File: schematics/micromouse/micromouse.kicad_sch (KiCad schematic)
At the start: 61 parts, among them J1 TOF_LEFT, J10 MotorB_Conn, J11 BMI_ConnB, J12 BMI_ConnA, J13 StepDown_{In+}, J14 StepDown_{In-}, J15 StepDown_{Out+}, J16 StepDown_{Out-}, J2 TOF_FRONTLEFT, J3 TOF_FRONTRIGHT, J4 TOF_RIGHT, J5 BatteryConnector, J6 PMW3360_Conn, J7 Bluetooth_Conn, J8 Programming_Conn, J9 MotorA_Conn, SW1 SW_SPDT, SW2 PB_RESET, SW3 PB_BOOT, SW4 SW_DIP_x04, U1 STM32F103CBTx, U2 DRV8833PWP, U3 AMS1117-3.3, U4 PCF8574TS, U5 PCF8574TS, U6 W25Q32JVSS, Y1 Crystal (8MHz), Y2 Crystal (8MHz)

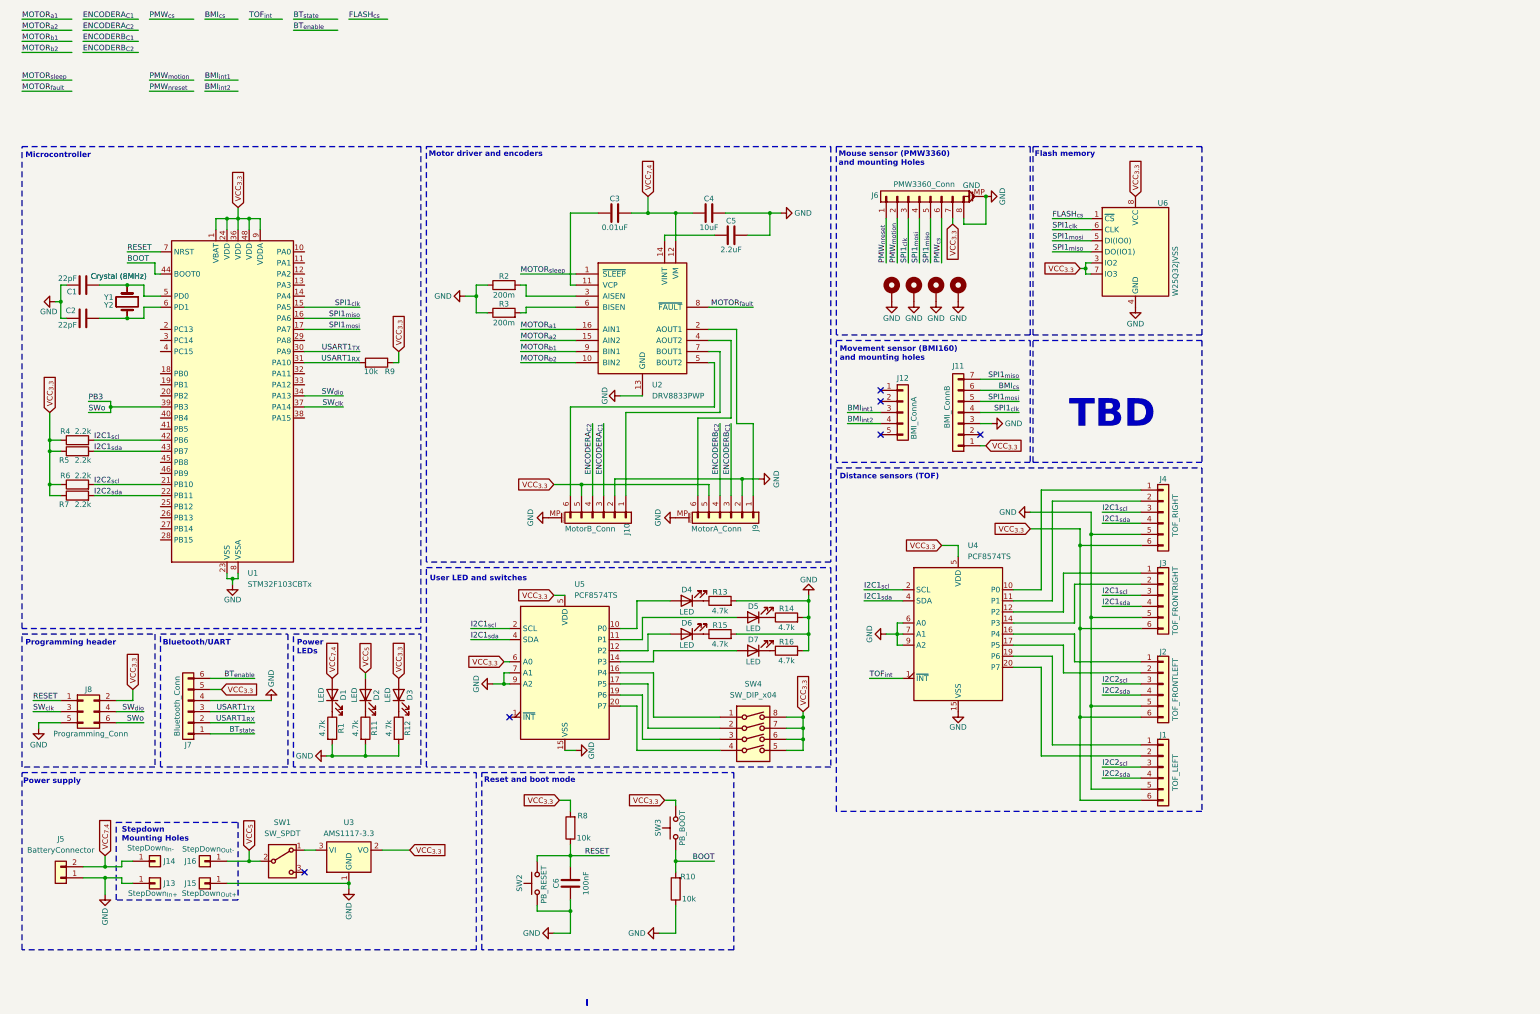
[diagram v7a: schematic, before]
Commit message: Schematic: * Reorganize STM32 pinout due to Software needs/mititations * Add PCB power protection diodes for Battery port and  Programming port.
PCB:
* Redistribute all lines
* Avoid Crystal zone with SPI/I2C lines
* Add text for element's pinouts

TODO: Add Test Points for signals?
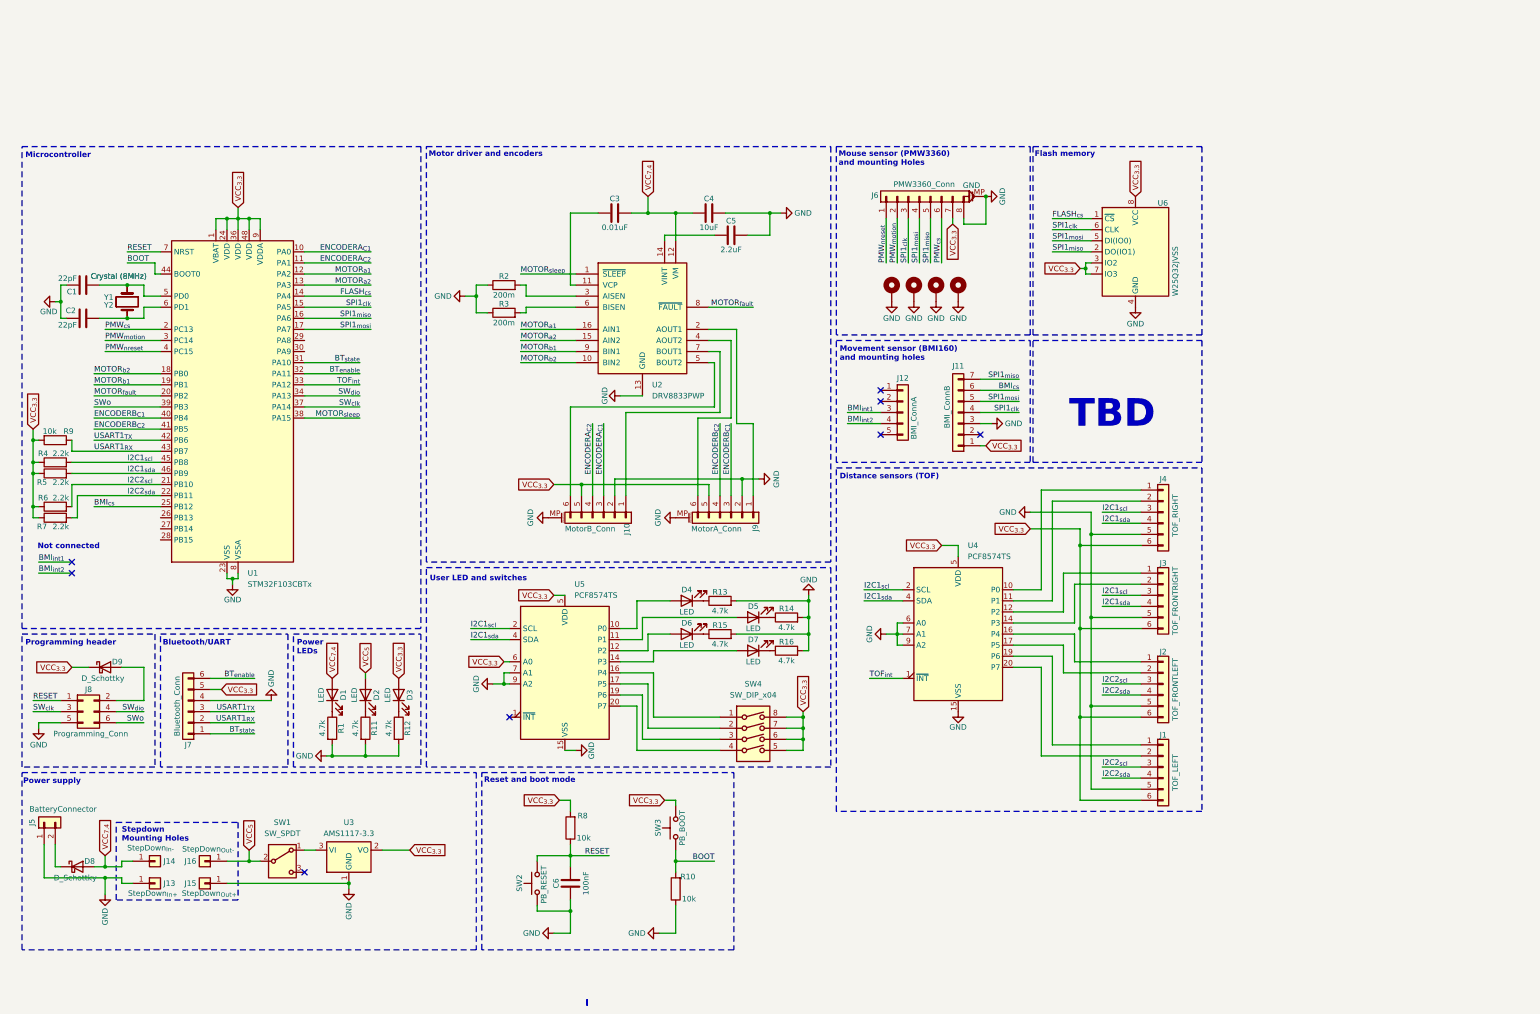
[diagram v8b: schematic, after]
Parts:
- added D8, D9: D_Schottky, Diode_SMD:D_SOD-123, symbol Device:D_Schottky
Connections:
- net VCC_{7,4} is gone; now on net VCC_{7.4}: C3.2, C4.1, U2.12 (VM)
- net BMI_{cs}: now also U1.25 (PB12)
- net BT_{enable}: now also U1.32 (PA11)
- net BT_{state}: now also U1.31 (PA10)
- net ENCODERA_{C1}: now also U1.10 (PA0)
- net ENCODERA_{C2}: now also U1.11 (PA1)
- net ENCODERB_{C1}: now also U1.40 (PB4)
- net ENCODERB_{C2}: now also U1.41 (PB5)
- net FLASH_{cs}: now also U1.14 (PA4)
- net I2C1_{scl}: now also U1.45 (PB8); no longer U1.42 (PB6)
- net I2C1_{sda}: now also U1.46 (PB9); no longer U1.43 (PB7)
- net MOTOR_{a1}: now also U1.12 (PA2)
- net MOTOR_{a2}: now also U1.13 (PA3)
- net MOTOR_{b1}: now also U1.19 (PB1)
- net MOTOR_{b2}: now also U1.18 (PB0)
- net MOTOR_{fault}: now also U1.20 (PB2)
- net MOTOR_{sleep}: now also U1.38 (PA15)
- net PMW_{cs}: now also U1.2 (PC13)
- net PMW_{motion}: now also U1.3 (PC14)
- net PMW_{nreset}: now also U1.4 (PC15)
- net TOF_{int}: now also U1.33 (PA12)
- net USART1_{RX}: now also R9.1, U1.43 (PB7); no longer R9.2, U1.31 (PA10)
- net USART1_{TX}: now also U1.42 (PB6); no longer U1.30 (PA9)
- net VCC_{3.3}: now also R9.2, D9.1 (K); no longer J8.2 (Pin_2), R9.1
- net VCC_{7.4}: now also D8.2 (A); no longer J5.2 (Pin_2)
- net PB3 renamed SWo
- new net: D9.2 (A), J8.2 (Pin_2)
- new net: D8.1 (K), J5.2 (Pin_2)
- no-connect marks 6 -> 8
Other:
- note added: "Not connected"
- moved on the sheet: J5, R4, R5, R6, R7
